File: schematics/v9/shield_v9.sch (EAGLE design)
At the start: 54 parts, among them IC1 L293DD, IC2 74HCT04D, Q2 PMV20EN, Q3 PMV20EN, Q4 PMV20EN, Q5 PMV20EN, U1 ATMEGA168

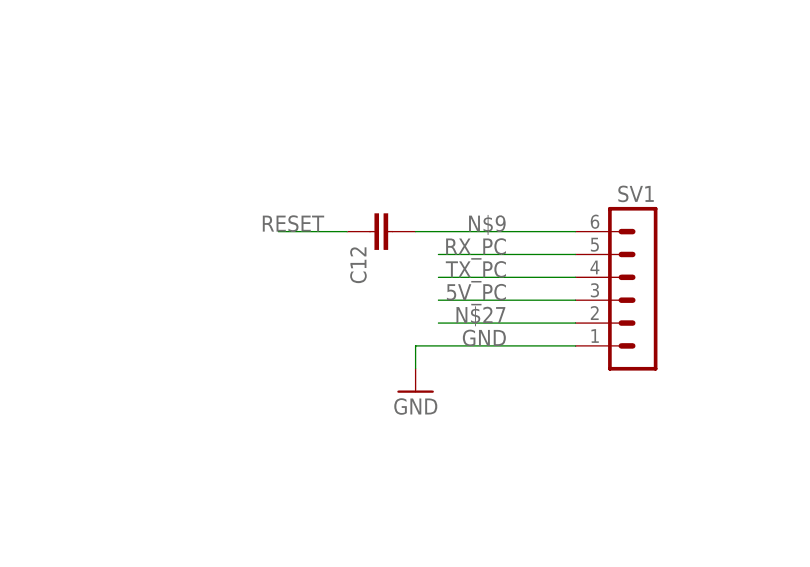
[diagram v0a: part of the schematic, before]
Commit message: added gerber files for ordered version
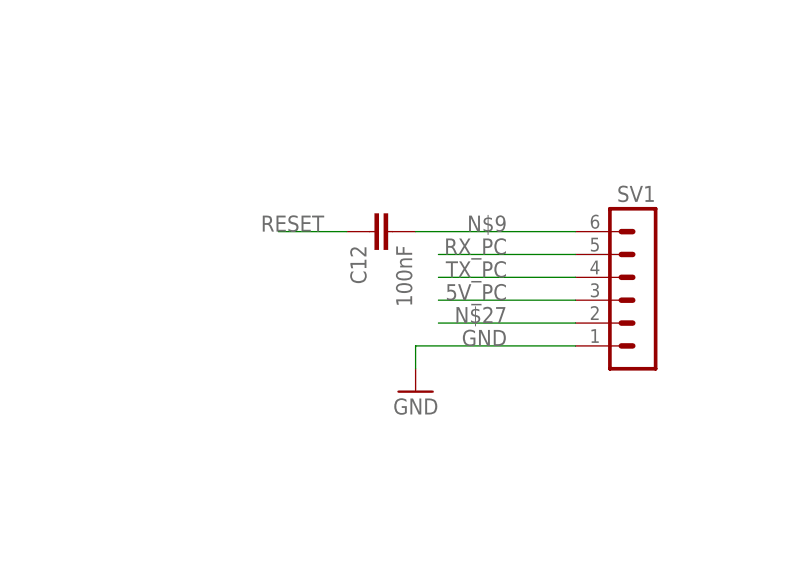
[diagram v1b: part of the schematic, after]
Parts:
- C12: value (none) -> 100nF
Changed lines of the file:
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@@
 <part name="PAD12" library="wirepad" deviceset="SMD2" device=""/>
 <part name="PAD13" library="wirepad" deviceset="SMD2" device=""/>
-<part name="C12" library="rcl" deviceset="C-EU" device="C1206"/>
+<part name="C12" library="rcl" deviceset="C-EU" device="C1206" value="100nF"/>
 <part name="SJ2" library="jumper" deviceset="SJ" device=""/>
 <part name="P+2" library="supply1" deviceset="VCC" device=""/>
